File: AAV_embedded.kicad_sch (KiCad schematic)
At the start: 37 parts, among them J1 JTAG_SWD_CONN, J2 12v in, J5 THR_EN_JMP, SW1 DAC_ADDR, SW2 IO_EXT_ADDR, SW3 SW_DIP_x03, SW5 DAC_ADDR, U1 DAC101C081CIMK, U2 PCA9555D, U3 LD1117S50TR_SOT223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

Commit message: board layout v1
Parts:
- removed 12vdecoup_H1: 0.1uF, Capacitor_SMD:C_1206_3216Metric, symbol Device:C_Small
- removed 12vdecoup_L1: 100uF, Capacitor_SMD:C_1206_3216Metric, symbol Device:C_Small
- removed 3.3vreg_Cin1, 5vreg_Cin2: 100nF, Capacitor_SMD:C_1206_3216Metric, symbol Device:C_Small
- removed 3.3vreg_Cout1, 5vreg_Cout2: 10uF, Capacitor_SMD:C_1206_3216Metric, symbol Device:C_Small
- removed D1: D_Schottky_low_forward, Diode_SMD:D_1206_3216Metric, symbol Device:D_Schottky
- removed D2: D_TVS, Diode_SMD:D_1206_3216Metric, symbol Device:D_TVS
- removed J2: 12v in, Connector_PinSocket_1.00mm:PinSocket_1x02_P1.00mm_Vertical, symbol PCM_4ms_Connector:Conn_01x02
- removed R1, R2: 2k, Resistor_SMD:R_1206_3216Metric, symbol Device:R
- removed S1: GPTS203211B, Button_Switch_SMD:SW_Push_1P1T_NO_CK_PTS125Sx43PSMTR, symbol dk_Pushbutton-Switches:GPTS203211B
- removed U3: LD1117S50TR_SOT223, Package_TO_SOT_SMD:SOT-223-3_TabPin2, symbol Regulator_Linear:LD1117S50TR_SOT223
- removed U4: LD1117S33TR_SOT223, Package_TO_SOT_SMD:SOT-223-3_TabPin2, symbol Regulator_Linear:LD1117S33TR_SOT223
- added R11, R12, R13, R14: 2k, Resistor_SMD:R_1206_3216Metric, symbol Device:R_US
- added SW6: ~{RESET_uMOD}, Button_Switch_SMD:SW_Push_SPST_NO_Alps_SKRK, symbol Switch:SW_Push
- added SW7: ~{BOOT_uMOD}, Button_Switch_SMD:SW_Push_SPST_NO_Alps_SKRK, symbol Switch:SW_Push
- added SW8: ~{RESET_BRK}, Button_Switch_SMD:SW_Push_SPST_NO_Alps_SKRK, symbol Switch:SW_Push
- added SW9: ~{RESET_STR}, Button_Switch_SMD:SW_Push_SPST_NO_Alps_SKRK, symbol Switch:SW_Push
- D3: footprint LED_SMD:LED_1206_3216Metric -> LED_SMD:LED_1206_3216Metric_Pad1.42x1.75mm_HandSolder
- SW5: value DAC_ADDR -> THR_EN
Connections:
- net +3.3V: now also R11.2, R12.2
- net +5V: now also R13.2, R14.2
- net GND: now also SW6.1, SW7.1, SW8.1, SW9.1
- net SCL_1_H: now also R13.1
- net SCL_1_L: now also R11.1
- net SDA _1_L: now also R12.1
- net SDA_1_H: now also R14.1
- net RX_DRV_5v: now reaches U5.12 (B7)
- net TX_DRV_5v: now reaches U5.13 (B6)
- net ERR_STR: now reaches U5.14 (B5)
- net ERR_STR_L: now reaches U5.7 (A5)
- net TX_DRV_L: now reaches U5.8 (A6)
- net RX_DRV_L: now reaches U5.9 (A7)
- net ERR_HIGH renamed ERR_BRK
- net ERR_HIGH_L renamed ERR_BRK_L
- net ERR_LOW renamed ~{ERR}
- net ERR_LOW_L renamed ~{ERR_L}
- net GPIO_EXT_7 renamed ~{RST_STR}
- net ~{RST_STR}: now also SW9.2
- net GPIO_EXT_8 renamed ~{RST_BRK}
- net ~{RST_BRK}: now also SW8.2
- net RST renamed ~{RESET_uMOD}
- net ~{RESET_uMOD}: now also SW6.2
- new net ~{BOOT_uMOD}: SW7.2
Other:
- added sheet ESP32_micromod (esp32_micromod.kicad_sch)
- note removed: "12v input filtering and protection"
- title: (none) -> AAV Edge Main
- moved on the sheet: SW5, U5

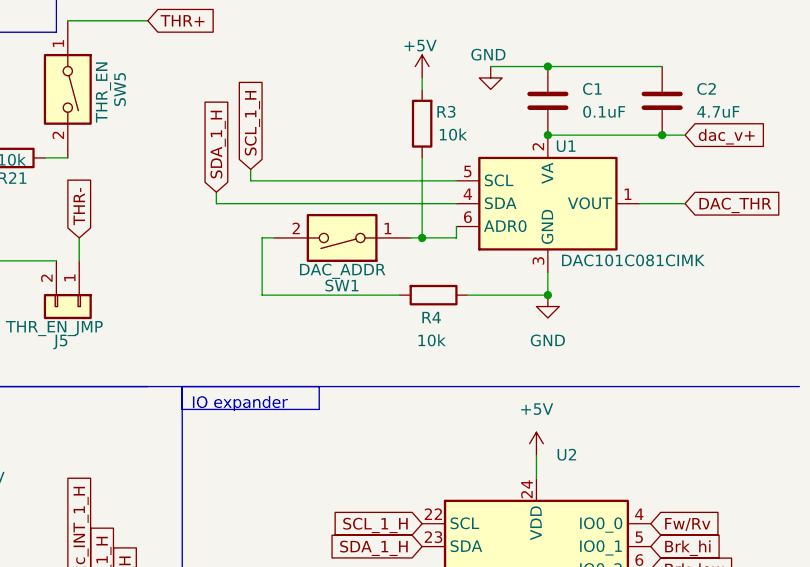
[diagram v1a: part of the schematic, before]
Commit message: i2c address fix and logo
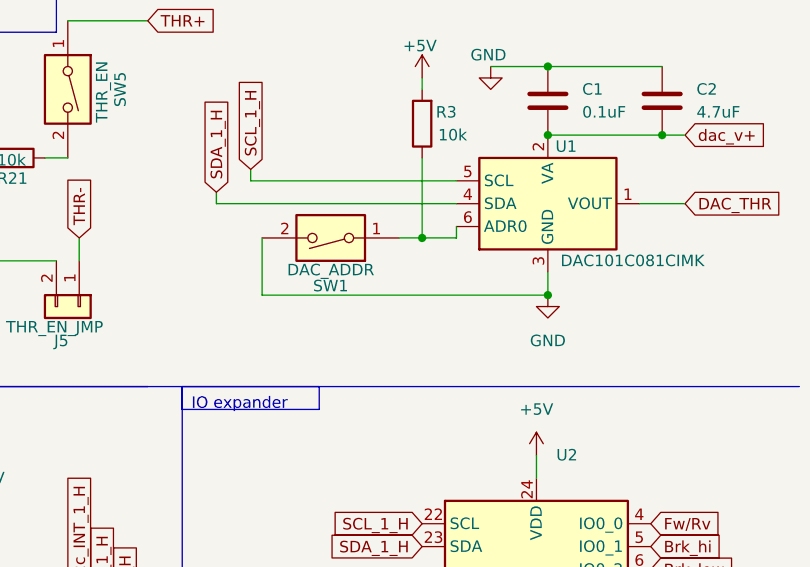
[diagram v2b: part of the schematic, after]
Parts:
- removed R4: 10k, Resistor_SMD:R_1206_3216Metric, symbol Device:R
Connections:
- net GND: now also SW1.2
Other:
- moved on the sheet: SW1
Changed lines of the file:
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@@
 	(wire
 		(pts
-			(xy 240.03 78.74) (xy 224.79 78.74)
+			(xy 224.79 78.74) (xy 256.54 78.74)
 		)
 		(stroke
@@
 	(wire
 		(pts
-			(xy 247.65 78.74) (xy 256.54 78.74)
-		)
-		(stroke
-			(width 0)
-			(type default)
-		)
-	)
-	(wire
-		(pts
 			(xy 269.24 25.4) (xy 269.24 24.13)
 		)
@@
 	(wire
 		(pts
-			(xy 241.3 72.39) (xy 242.57 72.39)
+			(xy 240.03 72.39) (xy 242.57 72.39)
 		)
 		(stroke
@@
 	(wire
 		(pts
-			(xy 224.79 72.39) (xy 226.06 72.39)
-		)
-		(stroke
-			(width 0)
-			(type default)
-		)
-	)
-	(wire
-		(pts
 			(xy 256.54 60.96) (xy 269.24 60.96)
 		)
@@
 	(symbol
 		(lib_id "Switch:SW_DIP_x01")
-		(at 233.68 72.39 180)
+		(at 232.41 72.39 180)
 		(unit 1)
 		(exclude_from_sim no)
@@
 		(dnp no)
 		(property "Reference" "SW1"
-			(at 233.68 77.724 0)
+			(at 232.41 77.724 0)
 			(effects
 				(font
@@
 		)
 		(property "Value" "DAC_ADDR"
-			(at 233.68 75.946 0)
+			(at 232.41 75.946 0)
 			(effects
 				(font
@@
 		)
 		(property "Footprint" "Button_Switch_SMD:SW_DIP_SPSTx01_Slide_6.7x4.1mm_W6.73mm_P2.54mm_LowProfile_JPin"
-			(at 233.68 72.39 0)
+			(at 232.41 72.39 0)
 			(effects
 				(font
@@
 		)
 		(property "Datasheet" "~"
-			(at 233.68 72.39 0)
+			(at 232.41 72.39 0)
 			(effects
 				(font
@@
 		)
 		(property "Description" "1x DIP Switch, Single Pole Single Throw (SPST) switch, small symbol"
-			(at 233.68 72.39 0)
+			(at 232.41 72.39 0)
 			(effects
 				(font
@@
 					(unit 1)
 				)
-			)
-		)
-	)
-	(symbol
-		(lib_id "Device:R")
-		(at 243.84 78.74 270)
-		(unit 1)
-		(exclude_from_sim no)
-		(in_bom yes)
-		(on_board yes)
-		(dnp no)
-		(property "Reference" "R4"
-			(at 243.586 81.28 90)
-			(effects
-				(font
-					(size 1.27 1.27)
-				)
-			)
-		)
-		(property "Value" "10k"
-			(at 243.586 83.82 90)
-			(effects
-				(font
-					(size 1.27 1.27)
-				)
-			)
-		)
-		(property "Footprint" "Resistor_SMD:R_1206_3216Metric"
-			(at 243.84 76.962 90)
-			(effects
-				(font
-					(size 1.27 1.27)
-				)
-				(hide yes)
-			)
-		)
-		(property "Datasheet" "~"
-			(at 243.84 78.74 0)
-			(effects
-				(font
-					(size 1.27 1.27)
-				)
-				(hide yes)
-			)
-		)
-		(property "Description" "Resistor"
-			(at 243.84 78.74 0)
-			(effects
-				(font
-					(size 1.27 1.27)
-				)
-				(hide yes)
-			)
-		)
-		(pin "1"
-		)
-		(pin "2"
-		)
-		(instances
-			(project "AAV_embedded"
-				(path "/00c590f3-503a-497c-946e-4acf8f8302df"
-					(reference "R4")
-					(unit 1)
-				)

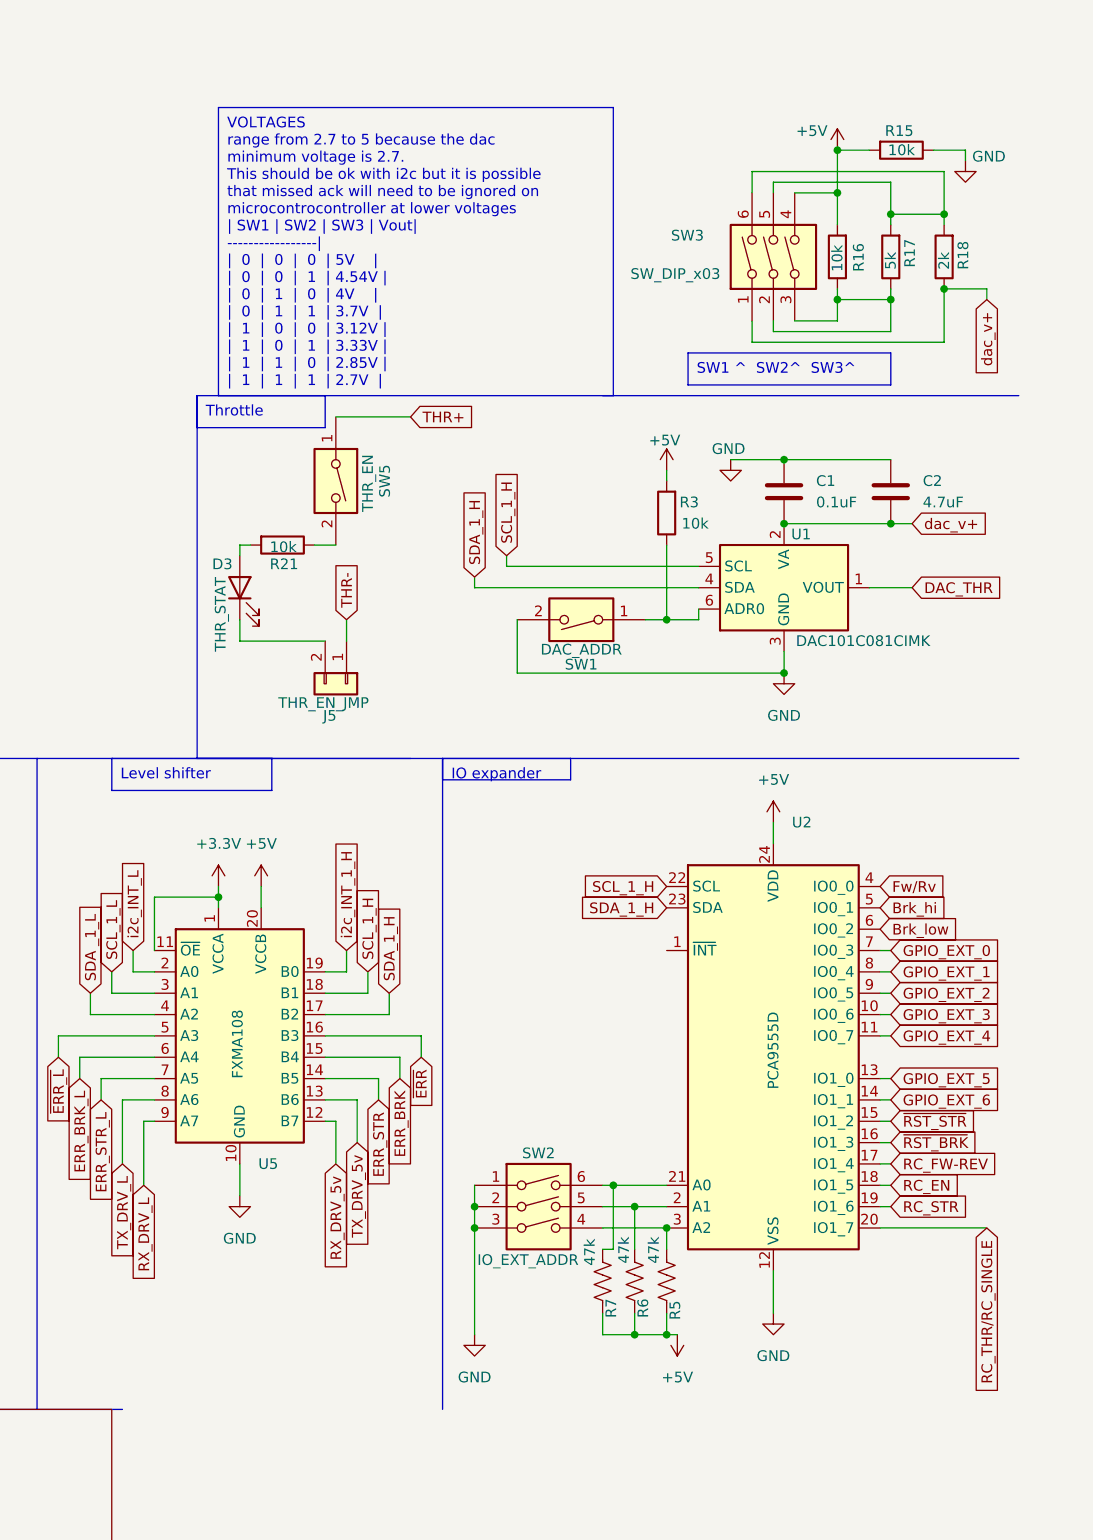
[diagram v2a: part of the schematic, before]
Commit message: Review and fixes from reliability and safety team
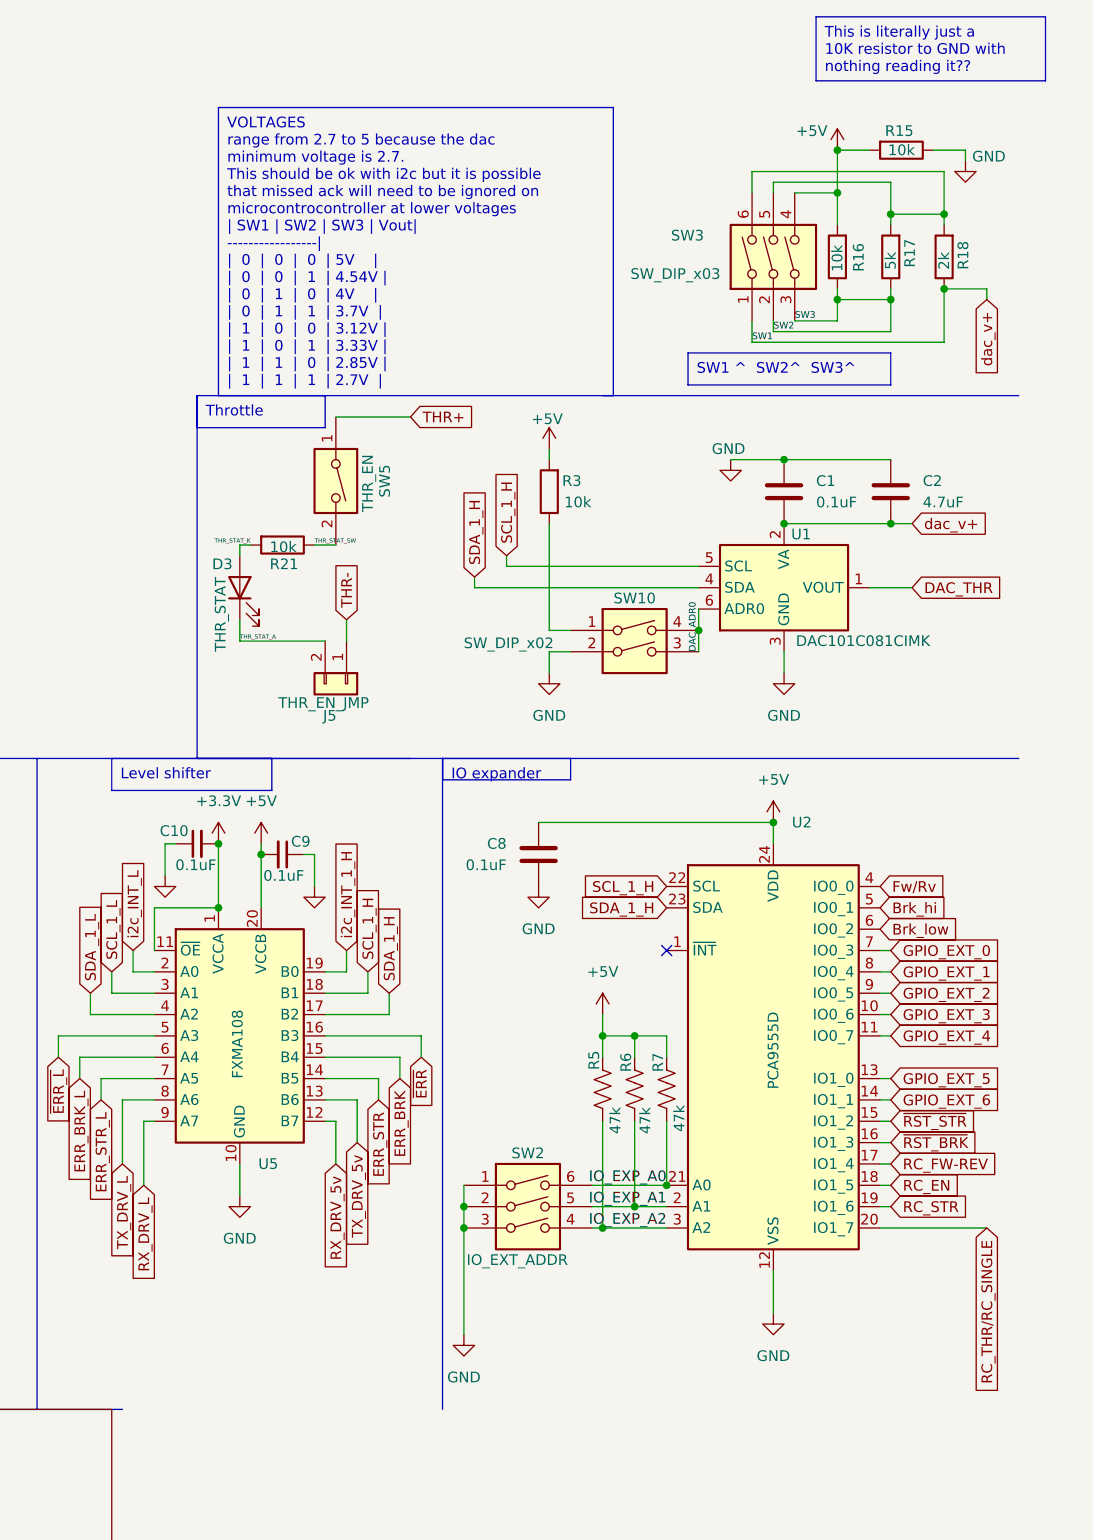
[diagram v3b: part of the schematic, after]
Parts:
- removed SW1: DAC_ADDR, Button_Switch_SMD:SW_DIP_SPSTx01_Slide_6.7x4.1mm_W6.73mm_P2.54mm_LowProfile_JPin, symbol Switch:SW_DIP_x01
- added C10, C9: 0.1uF, Capacitor_SMD:C_1206_3216Metric, symbol Device:C_Small
- added C8: 0.1uF, Capacitor_SMD:C_1206_3216Metric, symbol Device:C
- added SW10: SW_DIP_x02, Button_Switch_SMD:SW_DIP_SPSTx02_Slide_6.7x6.64mm_W6.73mm_P2.54mm_LowProfile_JPin, symbol Switch:SW_DIP_x02
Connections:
- net +3.3V: now also C10.2
- net +5V: now also C8.2, C9.2
- net GND: now also C10.1, C8.1, C9.1, SW10.2
- net THR_STAT_A: now reaches D3.1 (K), J5.2 (Pin_2)
- net IO_EXP_A0: now reaches R7.2, SW2.6, U2.21 (A0)
- net at R3.1: now also SW10.1; no longer U1.6 (ADR0)
- net SW2: now reaches R16.1, R17.1, SW3.2, SW3.3
- net IO_EXP_A2: now reaches R5.2, SW2.4, U2.3 (A2)
- net IO_EXP_A1: now reaches R6.2, SW2.5, U2.2 (A1)
- net THR_STAT_SW: now reaches R21.1, SW5.2
- net THR_STAT_K: now reaches D3.2 (A), R21.2
- new net DAC_ADR0: SW10.3, SW10.4, U1.6 (ADR0)
- no-connect marks 0 -> 1
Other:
- moved on the sheet: R3, R5, R6, R7, SW2

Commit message: added micromod breakout and fixed voltage divider
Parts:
- removed R16: 10k, Resistor_SMD:R_1206_3216Metric, symbol Device:R
- removed R17: 5k, Resistor_SMD:R_1206_3216Metric, symbol Device:R
- removed R18: 2k, Resistor_SMD:R_1206_3216Metric, symbol Device:R
- removed SW3: SW_DIP_x03, Button_Switch_SMD:SW_DIP_SPSTx03_Slide_6.7x9.18mm_W6.73mm_P2.54mm_LowProfile_JPin, symbol Switch:SW_DIP_x03
- added JP3: POT_HIGH_BYPASS, Jumper:SolderJumper-3_P1.3mm_Bridged12_Pad1.0x1.5mm, symbol Jumper:SolderJumper_3_Bridged12
- added JP4: POT_LOW_BYPASS, Jumper:SolderJumper-3_P1.3mm_Bridged12_Pad1.0x1.5mm, symbol Jumper:SolderJumper_3_Bridged12
- added POT1, POT2: TC33X-2-103E, Potentiometer_THT:Potentiometer_Bourns_3266W_Vertical, symbol dk_Trimmer-Potentiometers:TC33X-2-103E
- added R4: 10k, Resistor_SMD:R_1206_3216Metric, symbol Device:R
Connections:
- net +5V: now also JP3.2 (C); no longer R15.2
- net GND: now also POT2.2 (Wiper)
- net dac_v+: now also JP4.2 (C)
- new net: JP3.1 (A), POT1.1 (CCW)
- new net: JP4.1 (A), POT1.2 (Wiper), POT2.1 (CCW)
- new net: JP4.3 (B), R15.2, R4.1
- new net: JP3.3 (B), R4.2
- no-connect marks 1 -> 3
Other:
- removed sheet ESP32_micromod
- company: (none) -> Charlie Wadds

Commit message: changed LED
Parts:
- D3: footprint LED_SMD:LED_1206_3216Metric_Pad1.42x1.75mm_HandSolder -> LED_SMD:LED_0805_2012Metric
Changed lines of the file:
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@@
 			)
 		)
-		(property "Footprint" "LED_SMD:LED_1206_3216Metric_Pad1.42x1.75mm_HandSolder"
+		(property "Footprint" "LED_SMD:LED_0805_2012Metric"
 			(at 191.77 68.58 0)
 			(effects

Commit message: new branch with fixes
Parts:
- added J22, J4: ~, SparkFun-Connectors:JST-4-PTH, symbol SparkFun-Connectors:CONN_04JST-PTH
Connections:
- net +3.3V: now also J22.3
- net +5V: now also J4.3
- net GND: now also J22.4, J4.4
- net SCL_1_H: now also J4.1
- net SCL_1_L: now also J22.1
- net SDA _1_L: now also J22.2
- net SDA_1_H: now also J4.2
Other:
- note added: "i2c_3.3vv"
- note added: "i2c_5v"
- moved on the sheet: R11, R12, R13, R14

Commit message: fix level shifting in schematic
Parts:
- added C12, C7: 0.1uF, Capacitor_SMD:C_1206_3216Metric, symbol Device:C_Small
- added U4: TCA9406DC, Package_SO:Zetex_SM8, symbol Interface:TCA9406DC
- J4: footprint SparkFun-Connectors:JST-4-PTH -> Connector_JST:JST_XA_B04B-XASK-1_1x04_P2.50mm_Vertical
- J5: footprint Connector_PinHeader_1.27mm:PinHeader_1x02_P1.27mm_Horizontal -> Connector_PinHeader_2.54mm:PinHeader_1x02_P2.54mm_Horizontal
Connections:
- net +3.3V: now also C7.2, U4.3 (VCCA); no longer U5.11 (~{OE})
- net +5V: now also C12.2, U4.7 (VCCB)
- net GND: now also U5.11 (~{OE}), C12.1, C7.1, U4.2 (GND)
- net SCL_1_H: now also U4.8 (SCL_B); no longer U5.18 (B1)
- net SCL_1_L: now also U4.5 (SCL_A); no longer U5.3 (A1)
- net SDA _1_L: now also U4.4 (SDA_A); no longer U5.4 (A2)
- net SDA_1_H: now also U4.1 (SDA_B); no longer U5.17 (B2)
